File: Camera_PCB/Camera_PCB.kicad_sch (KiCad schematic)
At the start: 1 part

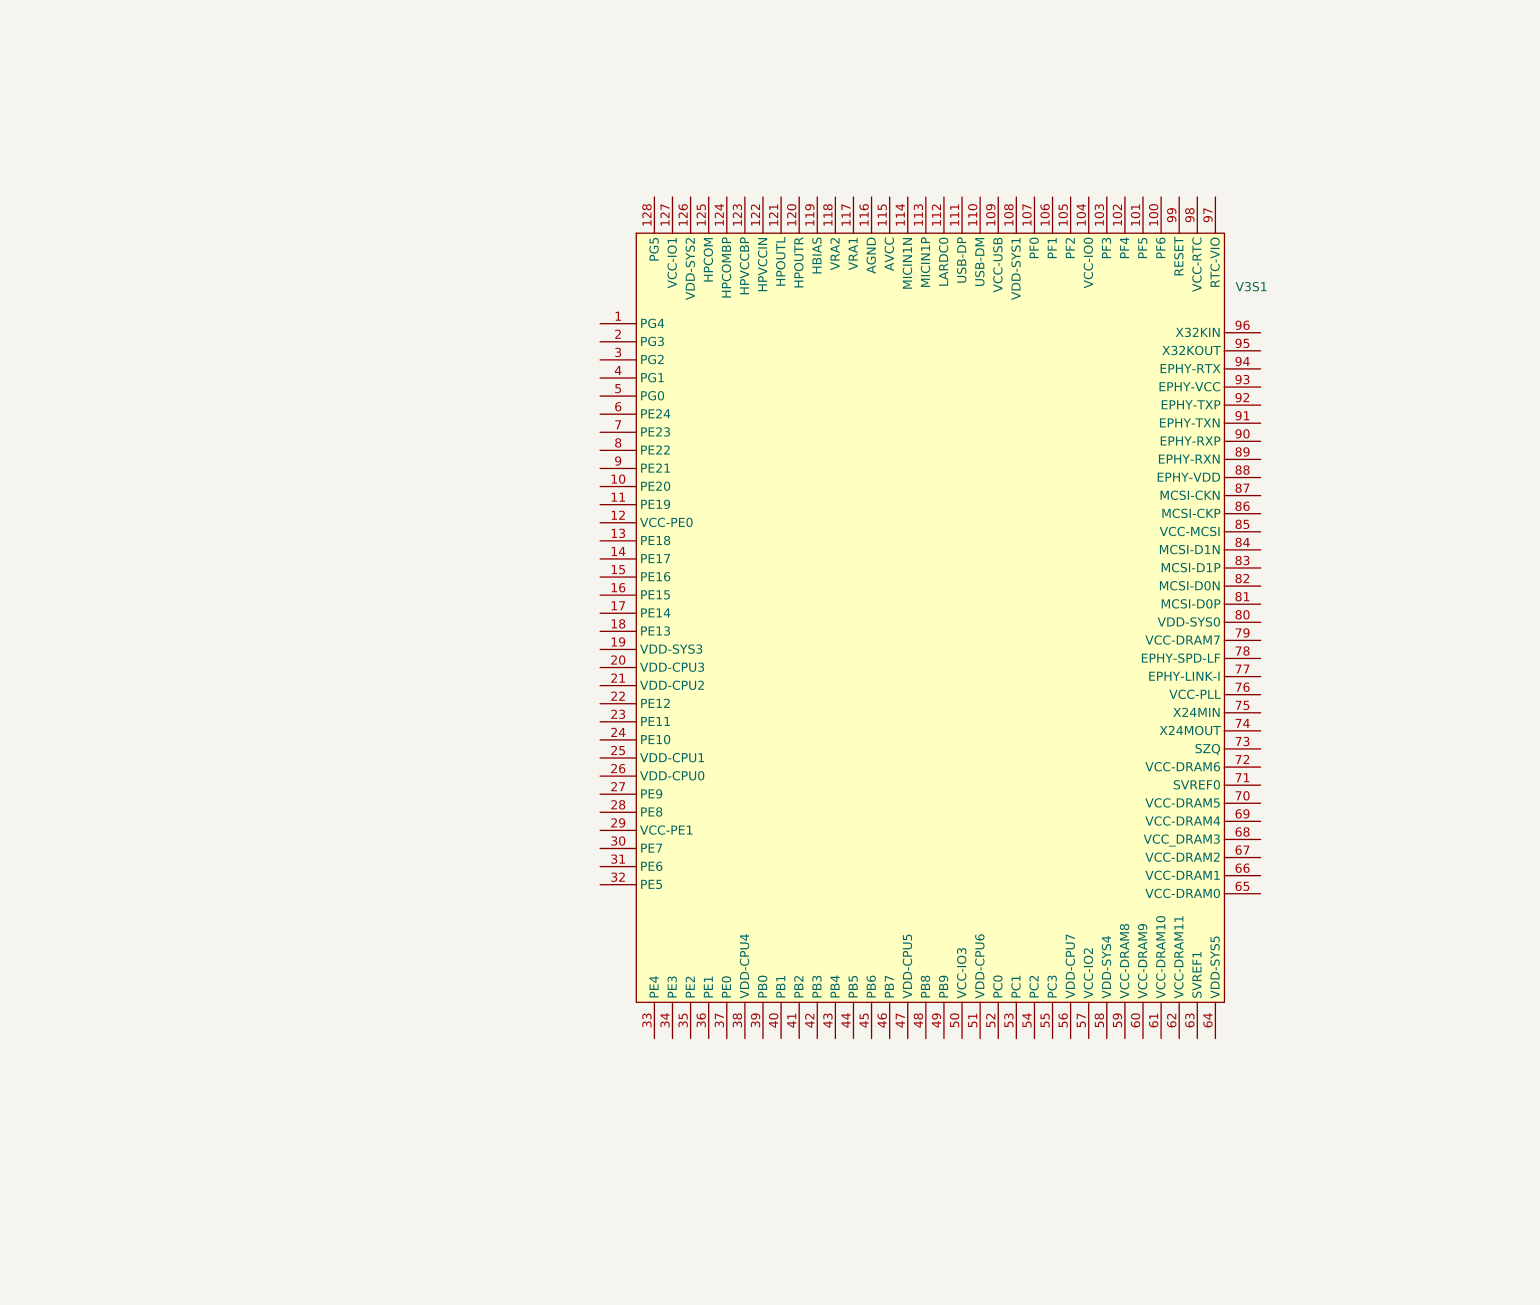
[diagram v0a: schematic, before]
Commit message: Modified symbol to inclued alternate pin descriptions
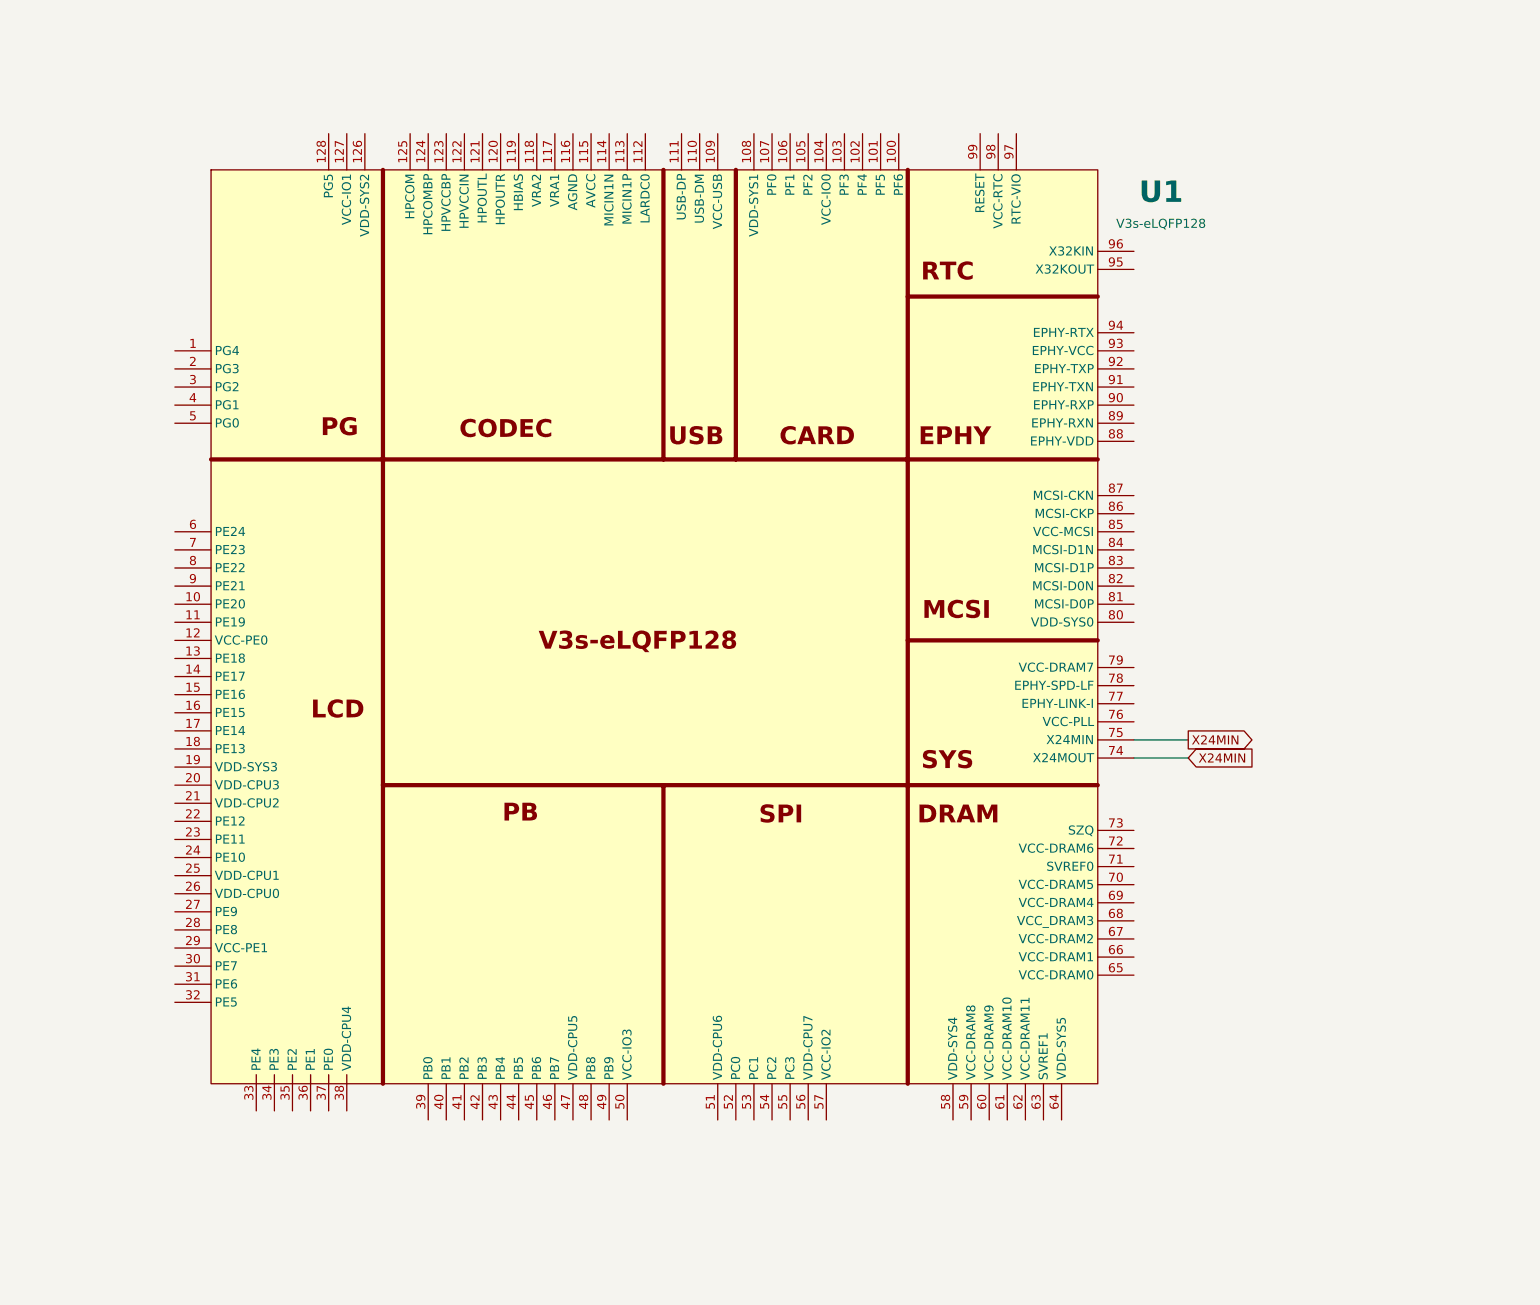
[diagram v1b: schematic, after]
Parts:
- removed V3S1: ~, symbol custom_chips:Allwinner-V3S
- added U1: V3s-eLQFP128, Package_QFP:LQFP-128_14x14mm_P0.4mm, symbol custom_chips:V3S-eLQFP128
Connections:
- new net X24MIN: U1.74 (X24MOUT), U1.75 (X24MIN)

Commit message: Added Most Power Inputs
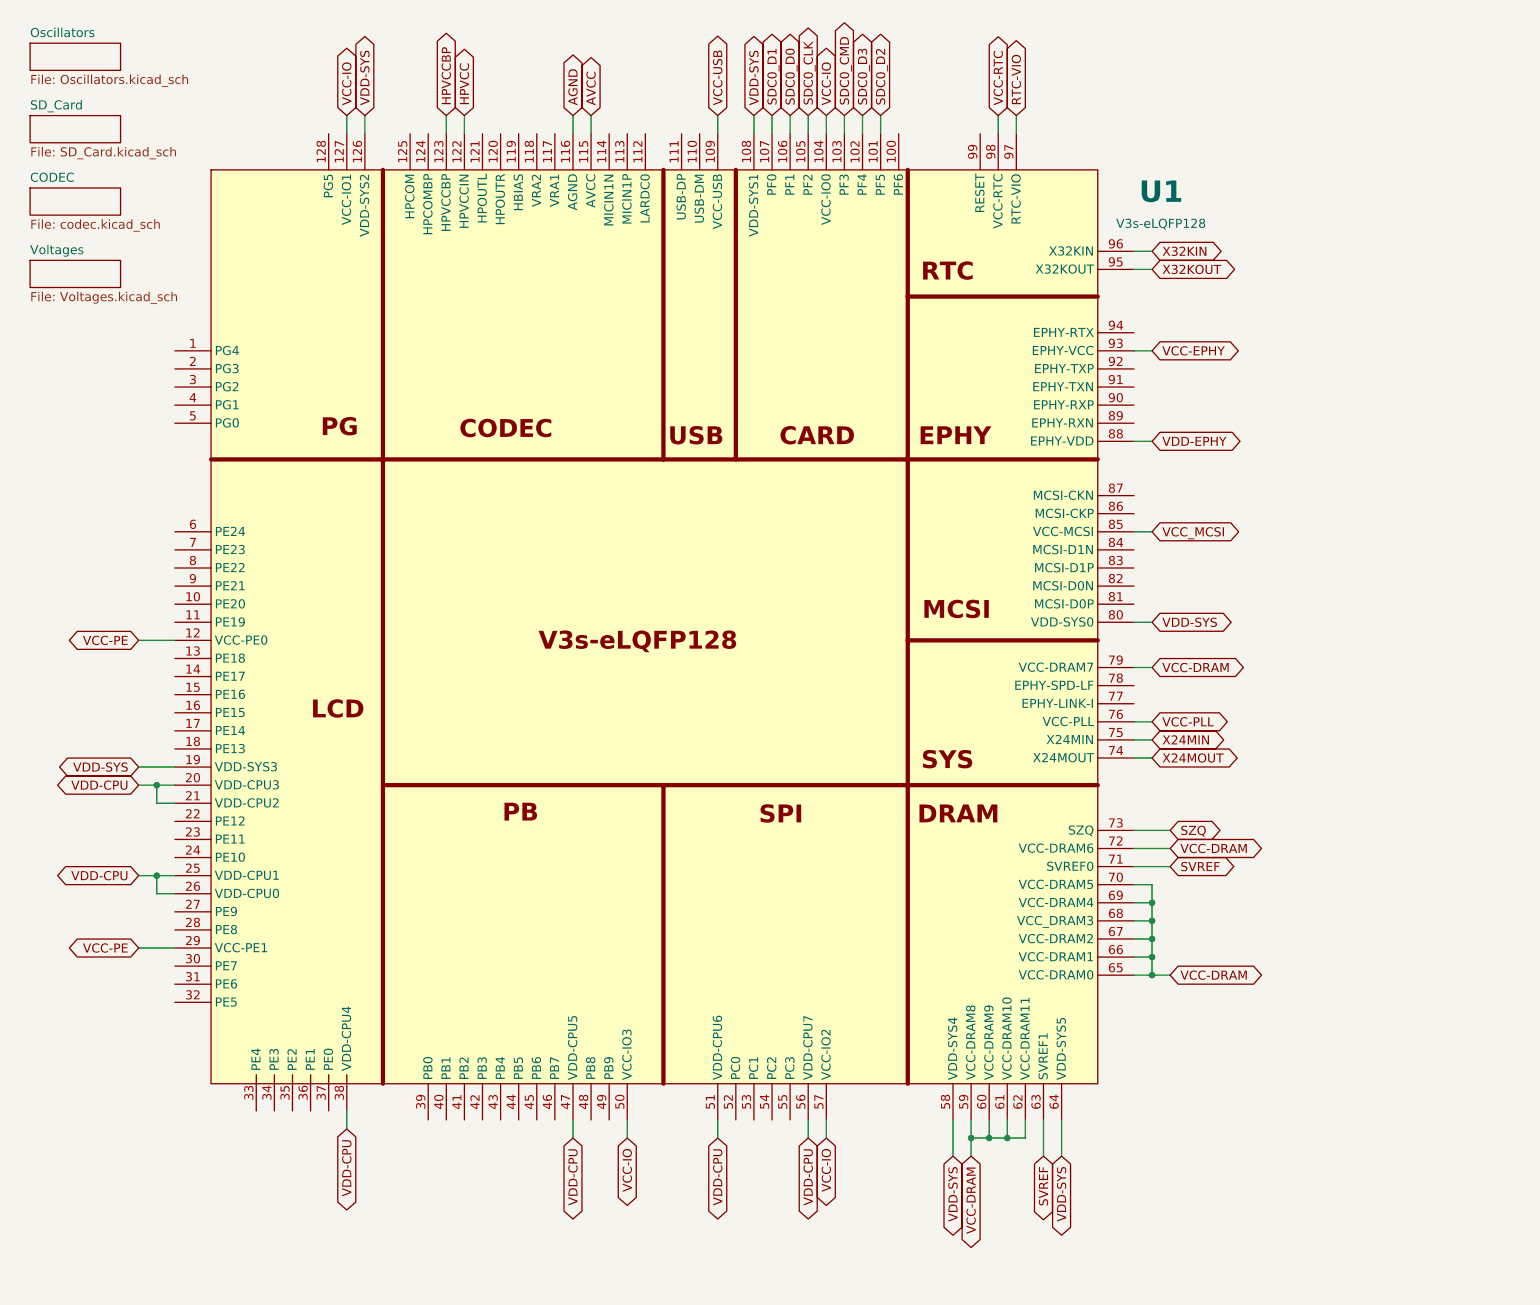
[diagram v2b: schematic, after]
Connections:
- net X24MIN: no longer U1.74 (X24MOUT)
- net SDC0_D2: now reaches U1.101 (PF5)
- net SDC0_D3: now reaches U1.102 (PF4)
- net SDC0_CMD: now reaches U1.103 (PF3)
- net VCC-IO: now reaches U1.104 (VCC-IO0)
- net VCC-IO: now also U1.127 (VCC-IO1), U1.50 (VCC-IO3), U1.57 (VCC-IO2)
- net SDC0_CLK: now reaches U1.105 (PF2)
- net SDC0_D0: now reaches U1.106 (PF1)
- net SDC0_D1: now reaches U1.107 (PF0)
- net VDD-SYS: now reaches U1.108 (VDD-SYS1)
- net VDD-SYS: now also U1.126 (VDD-SYS2), U1.19 (VDD-SYS3), U1.58 (VDD-SYS4), U1.64 (VDD-SYS5), U1.80 (VDD-SYS0)
- net VCC-USB: now reaches U1.109 (VCC-USB)
- net AVCC: now reaches U1.115 (AVCC)
- net AGND: now reaches U1.116 (AGND)
- net VCC-PE: now reaches U1.12 (VCC-PE0)
- net VCC-PE: now also U1.29 (VCC-PE1)
- net HPVCC: now reaches U1.122 (HPVCCIN)
- net HPVCCBP: now reaches U1.123 (HPVCCBP)
- net VDD-CPU: now reaches U1.20 (VDD-CPU3)
- net VDD-CPU: now also U1.21 (VDD-CPU2), U1.25 (VDD-CPU1), U1.26 (VDD-CPU0), U1.38 (VDD-CPU4), U1.47 (VDD-CPU5), U1.51 (VDD-CPU6), U1.56 (VDD-CPU7)
- net VCC-DRAM: now reaches U1.59 (VCC-DRAM8)
- net VCC-DRAM: now also U1.60 (VCC-DRAM9), U1.61 (VCC-DRAM10), U1.62 (VCC-DRAM11), U1.65 (VCC-DRAM0), U1.66 (VCC-DRAM1), U1.67 (VCC-DRAM2), U1.68 (VCC_DRAM3), U1.69 (VCC-DRAM4), U1.70 (VCC-DRAM5), U1.72 (VCC-DRAM6), U1.79 (VCC-DRAM7)
- net SVREF: now reaches U1.63 (SVREF1)
- net SVREF: now also U1.71 (SVREF0)
- net SZQ: now reaches U1.73 (SZQ)
- net VCC-PLL: now reaches U1.76 (VCC-PLL)
- net VCC_MCSI: now reaches U1.85 (VCC-MCSI)
- net VDD-EPHY: now reaches U1.88 (EPHY-VDD)
- net VCC-EPHY: now reaches U1.93 (EPHY-VCC)
- net X32KOUT: now reaches U1.95 (X32KOUT)
- net X32KIN: now reaches U1.96 (X32KIN)
- net RTC-VIO: now reaches U1.97 (RTC-VIO)
- net VCC-RTC: now reaches U1.98 (VCC-RTC)
- new net X24MOUT: U1.74 (X24MOUT)
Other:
- added sheet CODEC (codec.kicad_sch)
- added sheet Oscillators (Oscillators.kicad_sch)
- added sheet SD_Card (SD_Card.kicad_sch)
- added sheet Voltages (Voltages.kicad_sch)

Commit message: Schematic updates
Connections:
- net KEYADC0: now reaches U1.112 (LARDC0)
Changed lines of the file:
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@@
+	(wire
+		(pts
+			(xy 101.6 26.67) (xy 101.6 29.21)
+		)
+		(stroke
+			(width 0)
+			(type default)
+		)
+	)
 	(wire
 		(pts
@@
 			(effects
 				(font
+					(size 1.27 1.27)
+				)
+				(justify left)
+				(hide yes)
+			)
+		)
+	)
+	(global_label "KEYADC0"
+		(shape bidirectional)
+		(at 101.6 26.67 90)
+		(fields_autoplaced yes)
+		(effects
+			(font
+				(size 1.27 1.27)
+			)
+			(justify left)
+		)
+		(property "Intersheetrefs" "${INTERSHEET_REFS}"
+			(at 101.6 14.2278 90)
+			(effects
+				(font

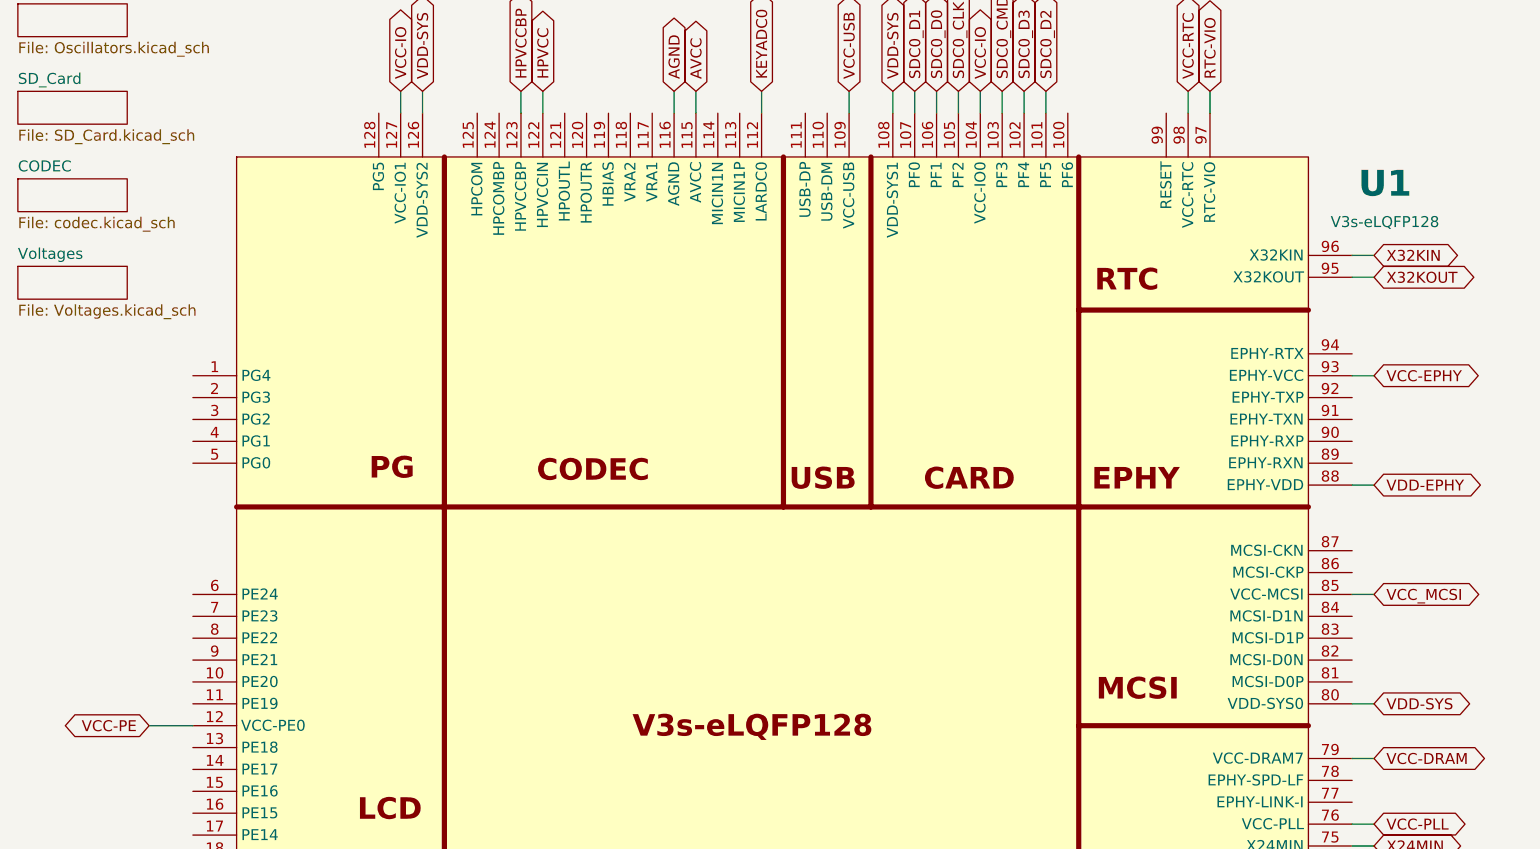
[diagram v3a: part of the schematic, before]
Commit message: Camera connections added
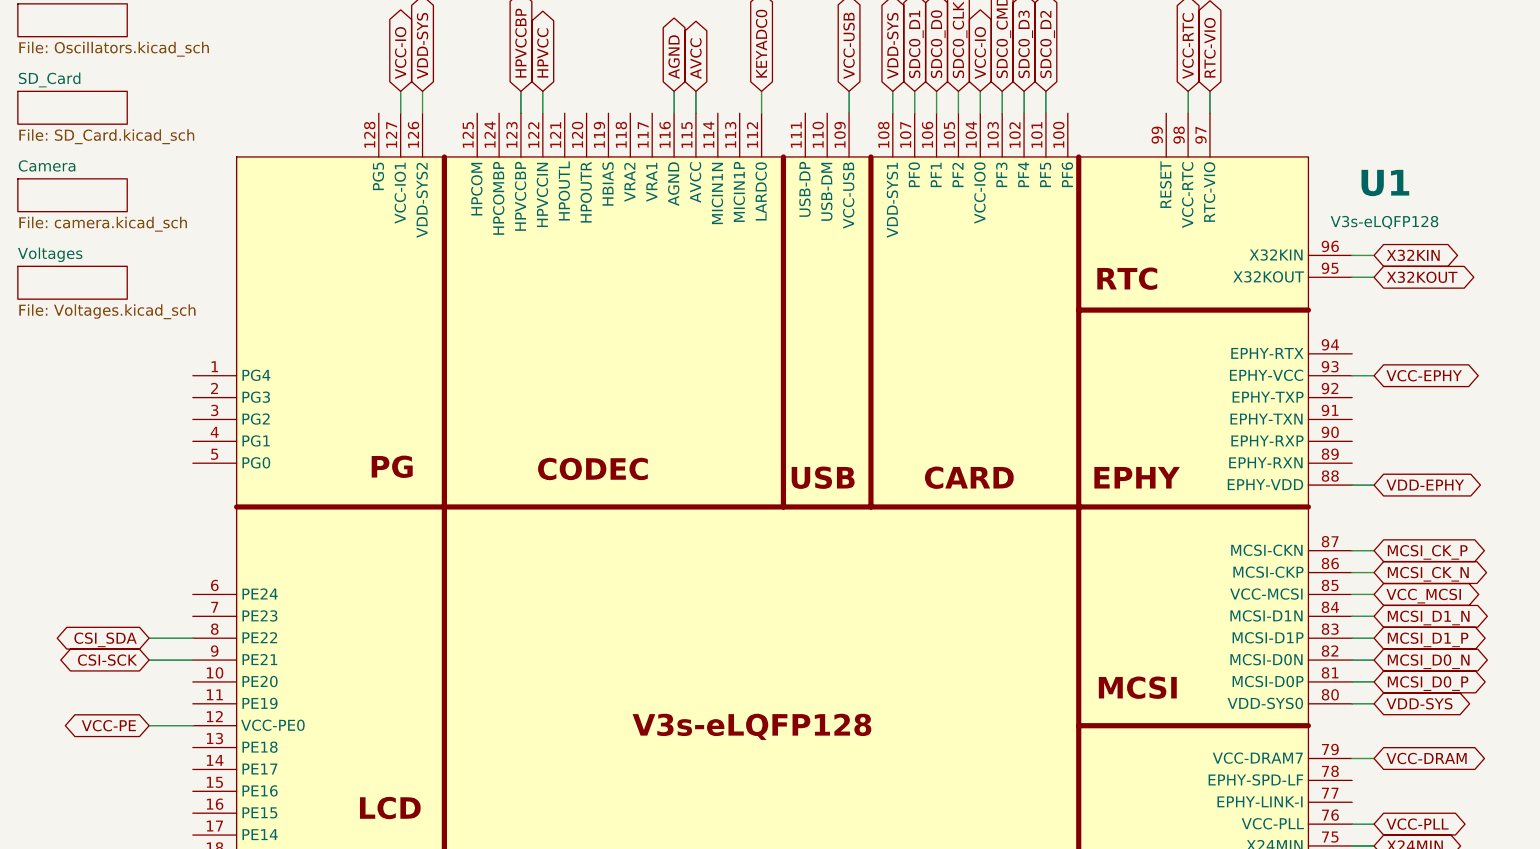
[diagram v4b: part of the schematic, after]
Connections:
- net CSI_SDA: now reaches U1.8 (PE22)
- net MCSI_D0_P: now reaches U1.81 (MCSI-D0P)
- net MCSI_D0_N: now reaches U1.82 (MCSI-D0N)
- net MCSI_D1_P: now reaches U1.83 (MCSI-D1P)
- net MCSI_D1_N: now reaches U1.84 (MCSI-D1N)
- net MCSI_CK_N: now reaches U1.86 (MCSI-CKP)
- net MCSI_CK_P: now reaches U1.87 (MCSI-CKN)
- net CSI-SCK: now reaches U1.9 (PE21)
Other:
- sheet CODEC renamed Camera
- sheet Camera: file codec.kicad_sch -> camera.kicad_sch
